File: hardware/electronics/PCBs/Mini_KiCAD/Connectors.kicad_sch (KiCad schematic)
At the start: 7 parts, among them J2 10118192-0001LF

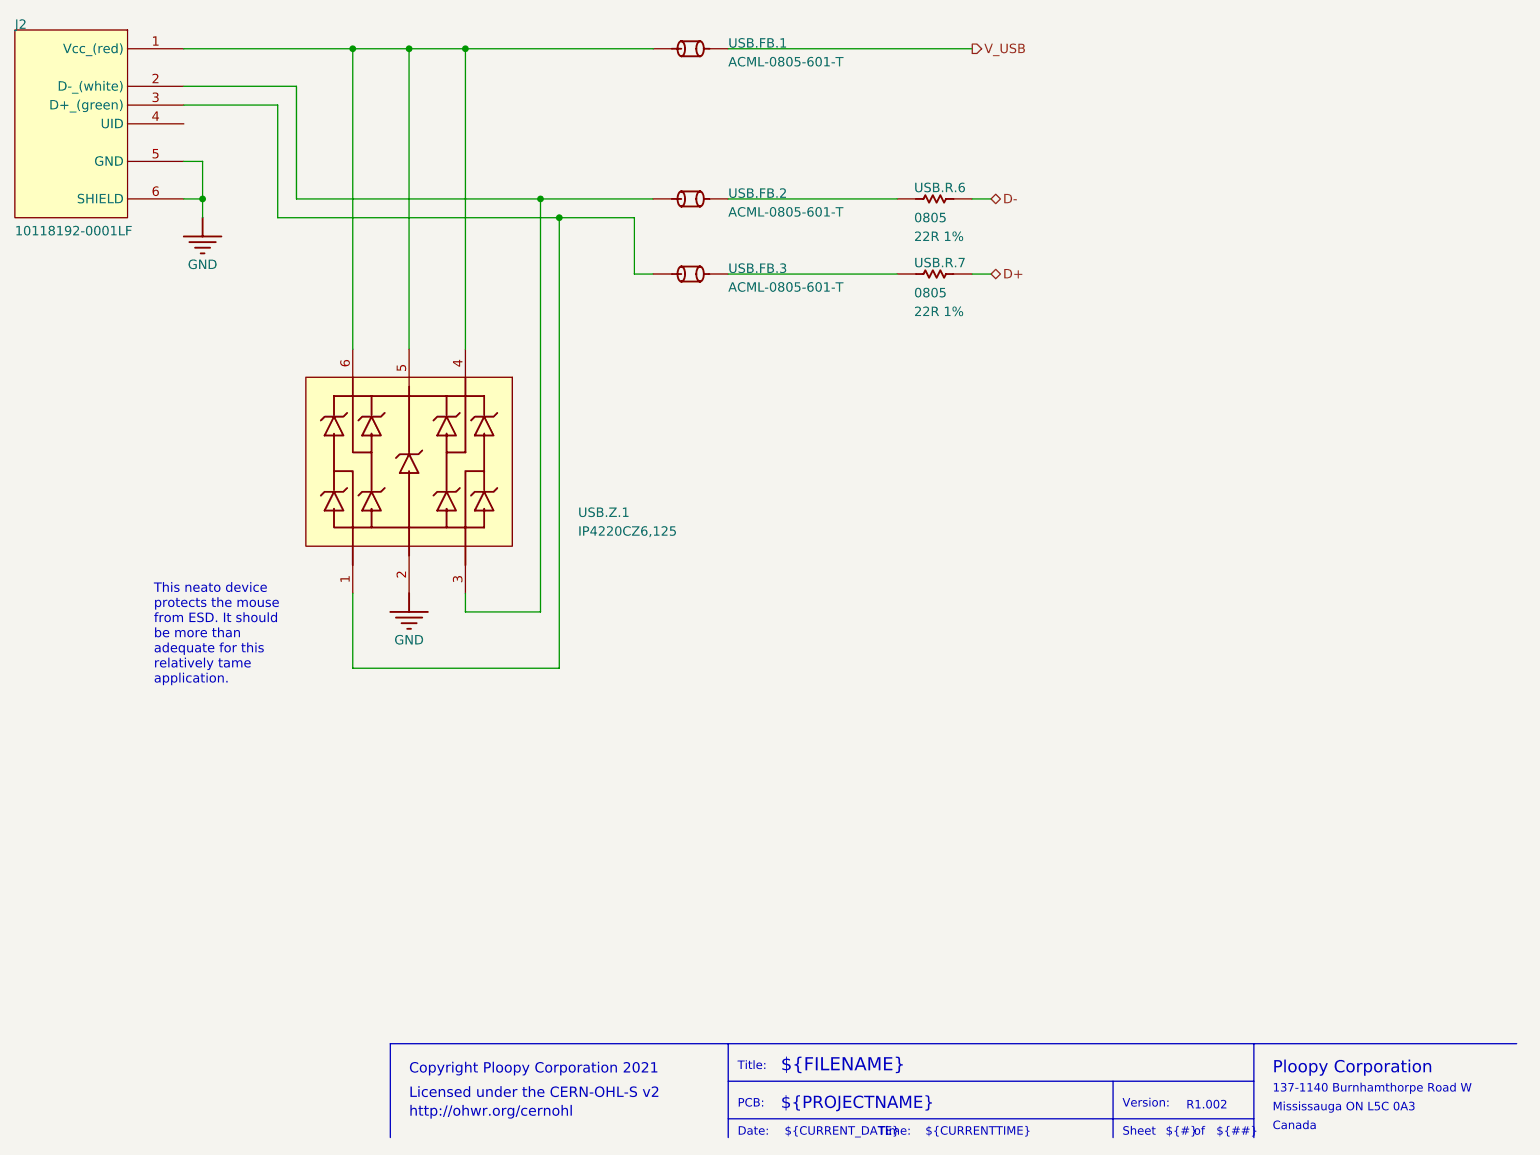
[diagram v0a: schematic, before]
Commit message: Initial commit of the PCB project file replacing the ADNS-5050 with PMW3360, referencing the schematic of the Ploopy Classic.
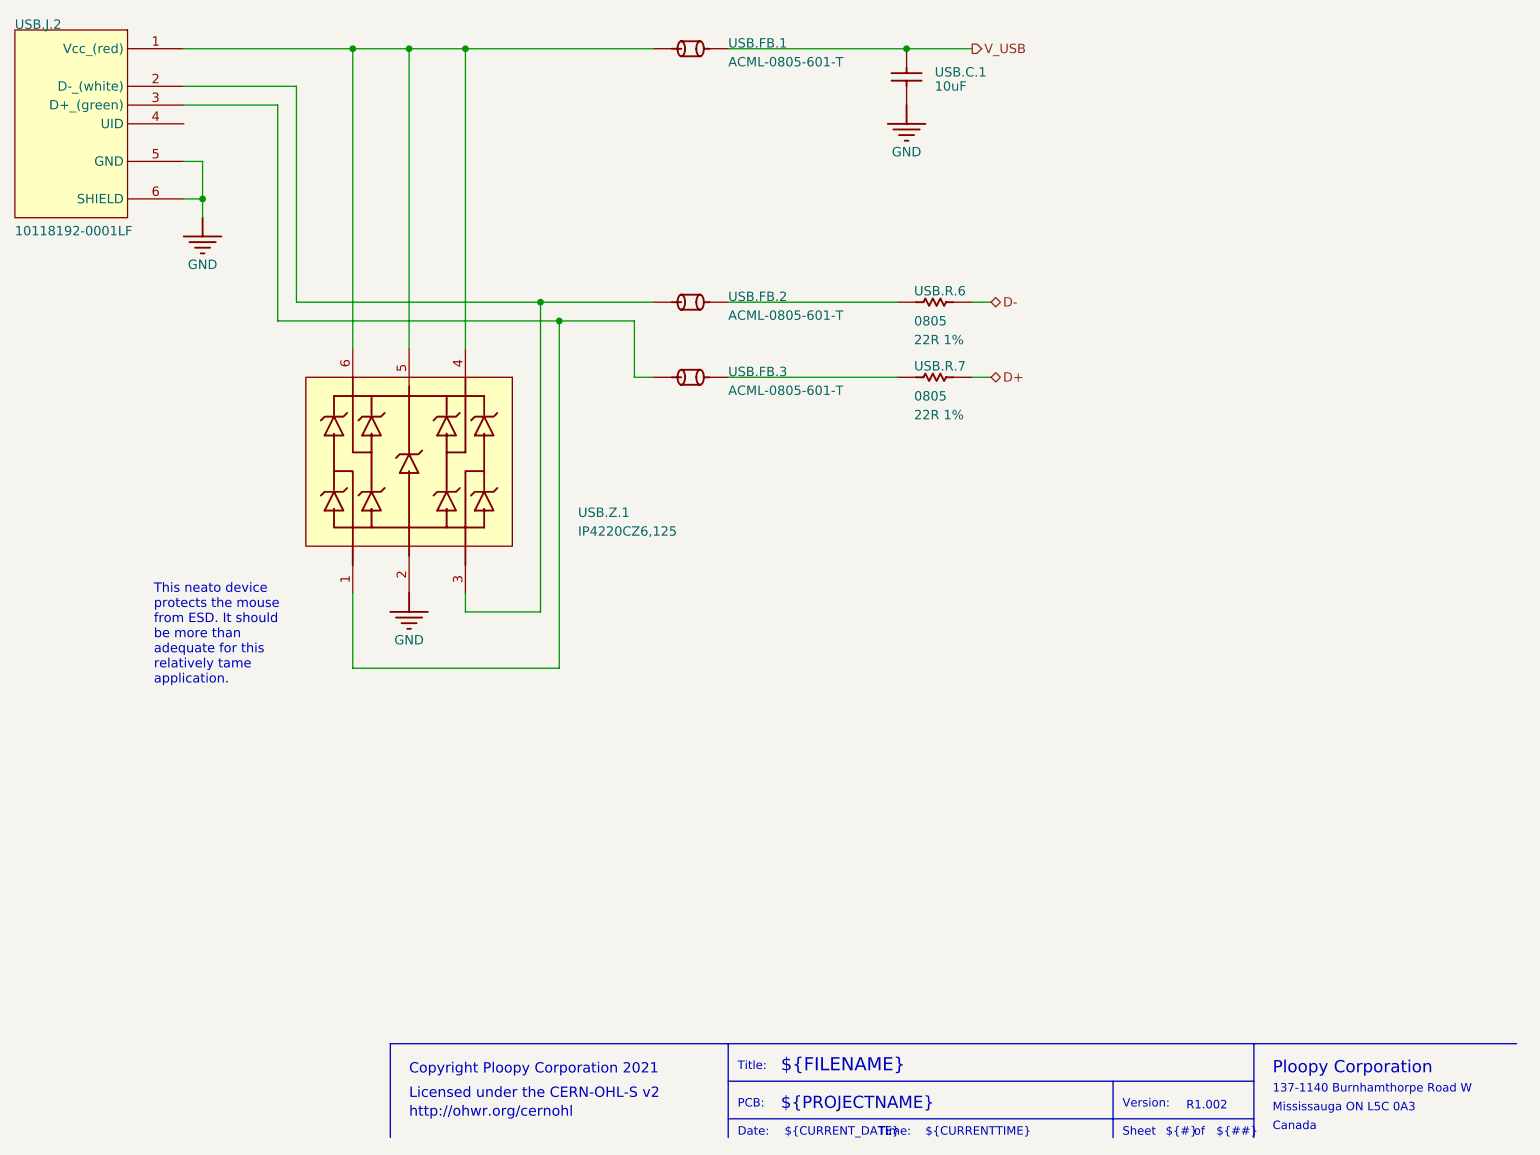
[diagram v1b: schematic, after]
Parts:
- added USB.C.1: 10uF, Chip_Passives.PcbLib:0805, symbol Mini-altium-import:MOS_1_Cap 10uF 25V
- USB.FB.1, USB.FB.2, USB.FB.3, USB.R.6, USB.R.7: footprint 0805 -> Chip_Passives.PcbLib:0805
- USB.J.2: renamed from J2; footprint 10118192-0001LF -> Connectors.PcbLib:10118192-0001LF
- USB.Z.1: footprint PESD3V3S4UD - SOT95P275X110-6N -> Diodes.PcbLib:PESD3V3S4UD - SOT95P275X110-6N
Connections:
- net GND: now also USB.C.1.1
- net V_USB: now also USB.C.1.2
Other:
- moved on the sheet: USB.FB.2, USB.FB.3, USB.R.6, USB.R.7
